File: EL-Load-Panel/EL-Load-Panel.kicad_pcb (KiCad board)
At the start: 2 copper layers, 127 x 53 mm, 40 parts, among them J1 Touchscreen, J2 Conn_02x08_Odd_Even, SW1 ON/OFF, U1 MCP23008-xSO

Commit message: Fixed Panel 1r1 and Power-MCU 2r2 versions
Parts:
- moved J2 5.00 mm to (199.3, 69.8)
- moved C4 4.00 mm to (145.7, 80.0)
- moved C5 4.00 mm to (136.9, 76.4)
- moved C7 4.00 mm to (145.8, 67.3)
- moved D1 4.00 mm to (123.7, 72.7)
- moved ENC1 4.00 mm to (145.9, 70.5)
- moved H4 4.00 mm to (128.1, 80.2)
- moved R10 4.00 mm to (136.9, 69.3)
- moved R12 4.00 mm to (149.1, 73.0)
- moved R13 4.00 mm to (149.1, 69.5)
- moved R18 4.00 mm to (129.9, 72.7)
- moved R4 4.00 mm to (161.3, 78.1)
- moved R5 4.00 mm to (161.3, 80.2)
- moved R6 4.00 mm to (149.1, 80.0)
- moved R7 4.00 mm to (136.9, 72.9)
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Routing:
- net +3V3: track 207.8 -> 224.3 mm
- net /encB: track 74.0 -> 64.5 mm
- net /DC: track 35.4 -> 41.5 mm
- net /sw4: track 88.8 -> 94.4 mm
- net /encA: track 74.7 -> 80.2 mm
- net /RESET: track 36.3 -> 41.7 mm
- net /MOSI: track 30.7 -> 36.0 mm
- net /BLK: track 42.6 -> 47.5 mm
- net /CS2: track 49.1 -> 53.9 mm
- net /PEN: track 55.9 -> 60.5 mm
- net /MISO: track 42.9 -> 47.5 mm
- net /CS1: track 49.1 -> 53.7 mm
- net /sw0: track 84.0 -> 87.6 mm
- net /SCLK: track 35.0 -> 38.5 mm
- net /encS: track 49.8 -> 52.9 mm
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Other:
- outline, holes or cut-outs redrawn

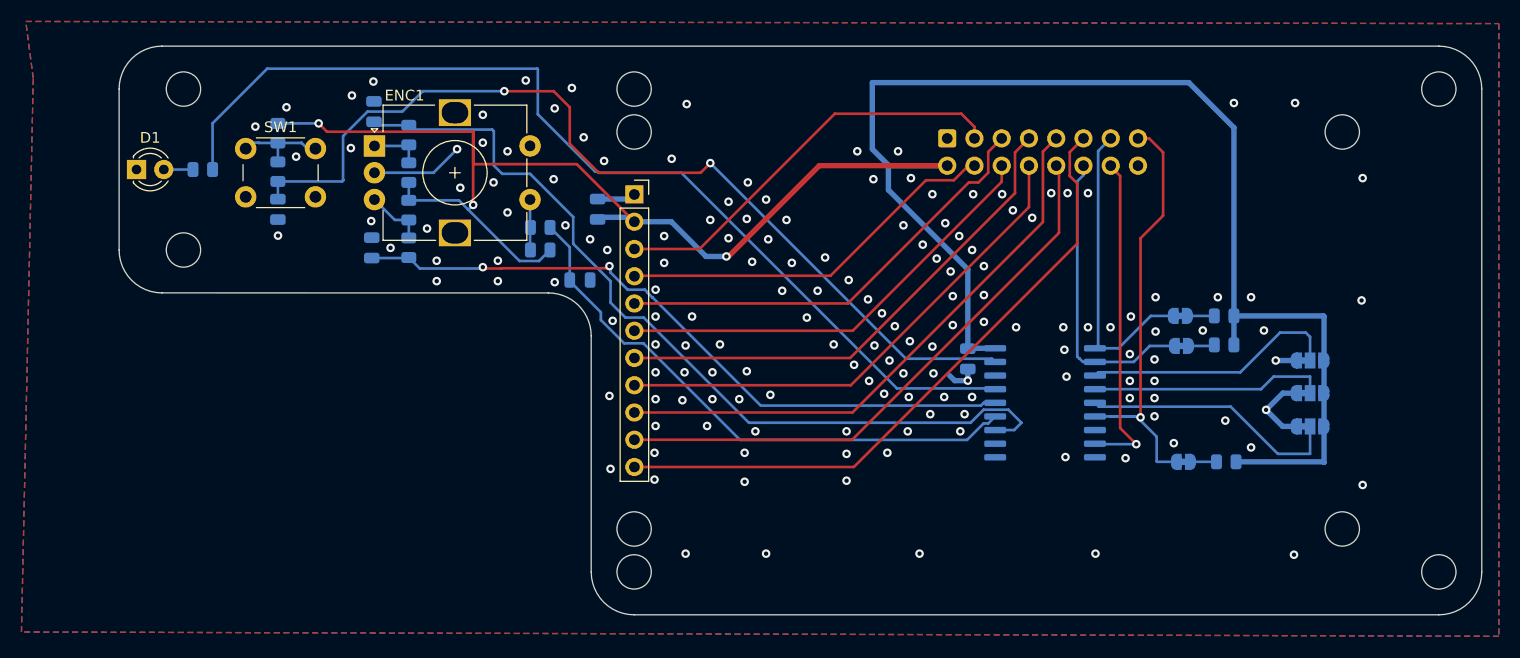
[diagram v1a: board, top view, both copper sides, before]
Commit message: Updated EL-Load-Panel to 1r2, fixing issues in issue #3.
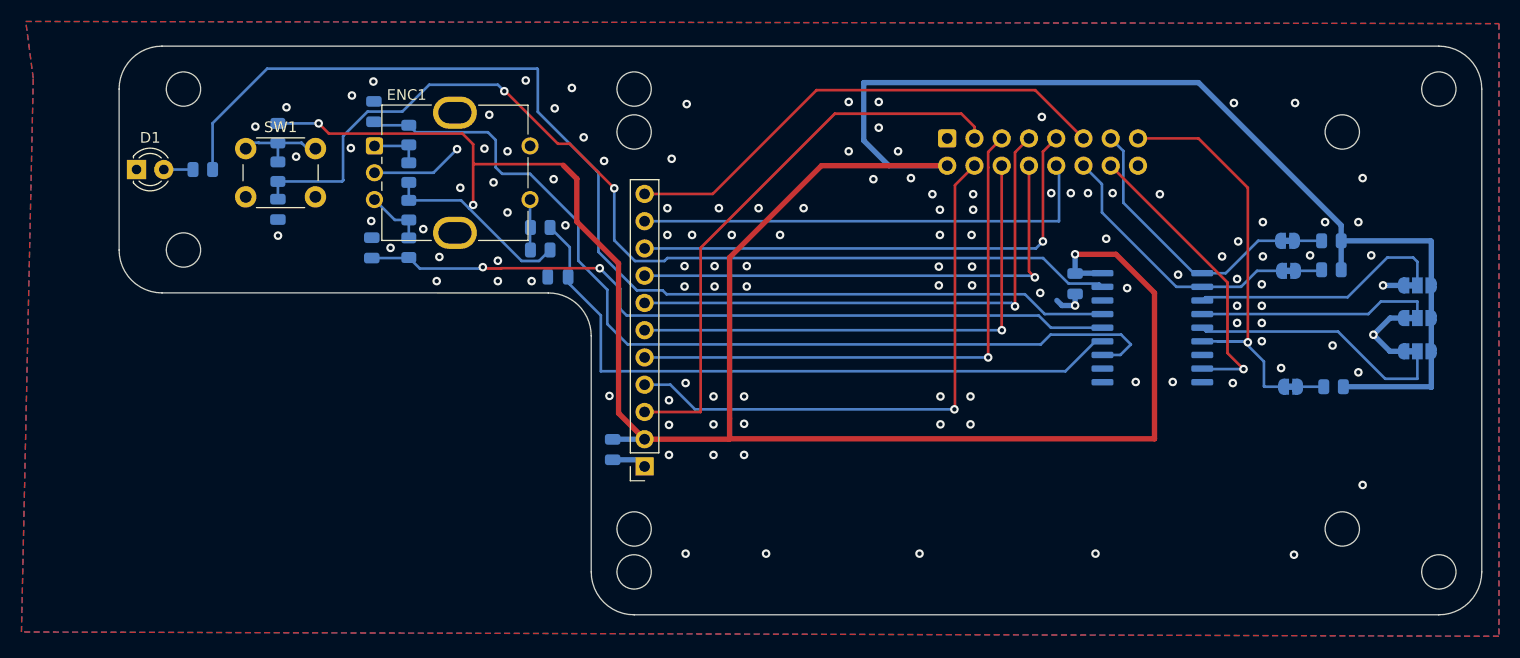
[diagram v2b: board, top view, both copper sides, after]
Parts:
- ENC1: footprint Rotary_Encoder:RotaryEncoder_Alps_EC12E-Switch_Vertical_H20mm -> Rotary_Encoder:RotaryEncoder_Bourns_Vertical_PEC12R-3x17F-Sxxxx
- moved J1 25.4 mm to (171.1, 100.4), turned to 180 degrees
- moved C1 22.4 mm to (168.1, 98.8), turned to -90 degrees
- moved C2 12.2 mm to (211.2, 83.3)
- moved JP1 12.2 mm to (243.1, 83.5)
- moved JP2 12.2 mm to (231.0, 79.3)
- moved JP3 12.2 mm to (243.1, 86.5)
- moved JP4 12.2 mm to (231.1, 82.1)
- moved JP5 12.2 mm to (243.1, 89.6)
- moved JP6 12.2 mm to (231.3, 92.9)
- moved R1 12.2 mm to (235.1, 79.3)
- moved R2 12.2 mm to (235.1, 82.0)
- moved R3 12.2 mm to (235.3, 92.9)
- moved U1 12.2 mm to (218.4, 87.4)
- moved C3 2.07 mm to (163.0, 82.7), turned to 180 degrees
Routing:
- net +3V3: track 224.3 -> 296.6 mm
- net /MOSI: track 36.0 -> 53.3 mm, vias 0 -> 1
- net /SCLK: track 38.5 -> 52.8 mm
- net /PEN: track 60.5 -> 46.8 mm
- net /sw4: track 94.4 -> 105.8 mm
- net /RESET: track 41.7 -> 53.0 mm, vias 0 -> 1
- net /encS: track 52.9 -> 63.3 mm
- net /CS2: track 53.9 -> 44.3 mm
- net /encA: track 80.2 -> 88.4 mm
- net /sw0: track 87.6 -> 95.6 mm
- net /encB: track 64.5 -> 72.1 mm
- net /DC: track 41.5 -> 48.7 mm, vias 0 -> 1
- net /CS1: track 53.7 -> 47.5 mm, vias 0 -> 1
- net /SCL: track 29.0 -> 25.3 mm
- net /BLK: track 47.5 -> 50.8 mm, vias 0 -> 1
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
